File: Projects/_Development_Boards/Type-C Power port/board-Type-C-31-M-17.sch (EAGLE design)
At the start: 2 parts, among them J1 TYPE-C-31-M-17

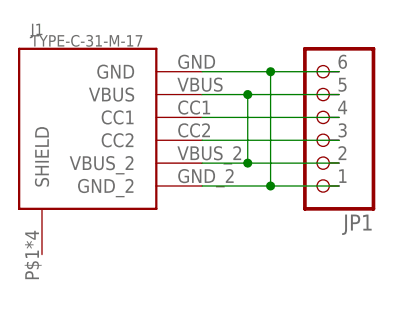
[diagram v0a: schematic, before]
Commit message: Type-C power port PCB panelized
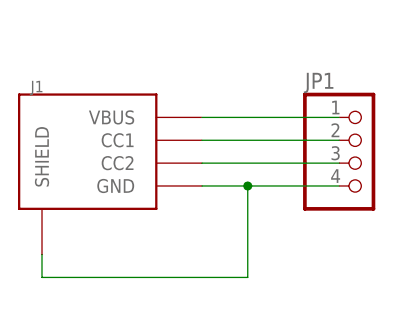
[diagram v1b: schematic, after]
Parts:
- J1: value TYPE-C-31-M-17 -> USB-TYPE-C-31-M-17; device angrypig7_Library:TYPE-C-31-M-17 -> angrypig7-Connectors:USB-TYPE-C-31-M-17
- JP1: device pinhead_v2:PINHD-1X6/OCT -> pinhead_v2:PINHD-1X4/OCT
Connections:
- net N$1: now also J1.GND, J1.SHIELD, JP1.4; no longer J1.VBUS, J1.VBUS_2, JP1.2, JP1.5
- net N$2: now also J1.VBUS; no longer J1.GND, J1.GND_2, JP1.6
- net N$3: now also JP1.2; no longer JP1.4
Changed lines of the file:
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@@
 <?xml version="1.0" encoding="utf-8"?>
 <!DOCTYPE eagle SYSTEM "eagle.dtd">
-<eagle version="9.5.2">
+<eagle version="9.6.0">
 <drawing>
 <settings>
-<setting alwaysvectorfont="yes"/>
+<setting alwaysvectorfont="no"/>
 <setting verticaltext="up"/>
 </settings>
@@
 <layer number="128" name="_bValues" color="7" fill="1" visible="no" active="no"/>
 <layer number="129" name="Mask" color="7" fill="1" visible="no" active="no"/>
+<layer number="130" name="SMDSTROOK" color="7" fill="1" visible="no" active="no"/>
 <layer number="131" name="tAdjust" color="7" fill="1" visible="no" active="no"/>
 <layer number="132" name="bAdjust" color="7" fill="1" visible="no" active="no"/>
+<layer number="133" name="bottom_silk" color="7" fill="1" visible="no" active="no"/>
+<layer number="134" name="silk_top" color="7" fill="1" visible="no" active="no"/>
+<layer number="135" name="silk_bottom" color="7" fill="1" visible="no" active="no"/>
+<layer number="136" name="silktop" color="7" fill="1" visible="no" active="yes"/>
+<layer number="137" name="silkbottom" color="7" fill="1" visible="no" active="yes"/>
 <layer number="144" name="Drill_legend" color="7" fill="1" visible="no" active="no"/>
+<layer number="145" name="DrillLegend_01-16" color="7" fill="1" visible="no" active="yes"/>
+<layer number="146" name="DrillLegend_01-20" color="7" fill="1" visible="no" active="yes"/>
 <layer number="150" name="Notes" color="7" fill="1" visible="no" active="no"/>
 <layer number="151" name="HeatSink" color="7" fill="1" visible="no" active="no"/>
@@
 <layer number="154" name="FabDoc2" color="7" fill="1" visible="no" active="no"/>
 <layer number="155" name="FabDoc3" color="7" fill="1" visible="no" active="no"/>
+<layer number="166" name="AntennaArea" color="7" fill="1" visible="no" active="yes"/>
+<layer number="168" name="4mmHeightArea" color="7" fill="1" visible="no" active="yes"/>
 <layer number="199" name="Contour" color="7" fill="1" visible="no" active="no"/>
 <layer number="200" name="200bmp" color="1" fill="10" visible="no" active="no"/>
@@
 </variantdefs>
 <classes>
-<class number="0" name="default" width="0" drill="0">
+<class number="0" name="default" width="0.254" drill="0">
+</class>
+<class number="1" name="power" width="0.4572" drill="0">
 </class>
 </classes>
 <parts>
-<part name="J1" library="angrypig7_Library" deviceset="TYPE-C-31-M-17" device=""/>
-<part name="JP1" library="pinhead_v2" deviceset="PINHD-1X6" device="/OCT"/>
+<part name="J1" library="angrypig7-Connectors" deviceset="USB-TYPE-C-31-M-17" device=""/>
+<part name="JP1" library="pinhead_v2" deviceset="PINHD-1X4" device="/OCT"/>
 </parts>
 <sheets>
@@
 </plain>
 <instances>
-<instance part="J1" gate="G$1" x="7.62" y="25.4" smashed="yes">
-<attribute name="NAME" x="6.35" y="34.544" size="1.27" layer="95"/>
-<attribute name="VALUE" x="6.35" y="33.274" size="1.27" layer="95"/>
+<instance part="J1" gate="G$1" x="7.62" y="20.32" smashed="yes">
+<attribute name="NAME" x="6.35" y="28.194" size="1.27" layer="95"/>
 </instance>
-<instance part="JP1" gate="A" x="38.1" y="25.4" smashed="yes" rot="R180">
-<attribute name="NAME" x="44.45" y="14.605" size="1.778" layer="95" rot="R180"/>
-<attribute name="VALUE" x="44.45" y="35.56" size="1.778" layer="96" rot="R180"/>
+<instance part="JP1" gate="A" x="43.18" y="20.32" smashed="yes">
+<attribute name="NAME" x="36.83" y="28.575" size="1.778" layer="95"/>
+<attribute name="VALUE" x="36.83" y="12.7" size="1.778" layer="96"/>
 </instance>
 </instances>
@@
 </busses>
 <nets>
-<net name="N$1" class="0">
+<net name="N$1" class="1">
+<segment>
+<pinref part="J1" gate="G$1" pin="SHIELD"/>
+<wire x1="7.62" y1="10.16" x2="7.62" y2="7.62" width="0.1524" layer="91"/>
+<wire x1="7.62" y1="7.62" x2="30.48" y2="7.62" width="0.1524" layer="91"/>
+<wire x1="30.48" y1="7.62" x2="30.48" y2="17.78" width="0.1524" layer="91"/>
+<pinref part="J1" gate="G$1" pin="GND"/>
+<wire x1="30.48" y1="17.78" x2="25.4" y2="17.78" width="0.1524" layer="91"/>
+<pinref part="JP1" gate="A" pin="4"/>
+<wire x1="30.48" y1="17.78" x2="40.64" y2="17.78" width="0.1524" layer="91"/>
+<junction x="30.48" y="17.78"/>
+</segment>
+</net>
+<net name="N$2" class="1">
 <segment>
 <pinref part="J1" gate="G$1" pin="VBUS"/>
-<wire x1="25.4" y1="27.94" x2="30.48" y2="27.94" width="0.1524" layer="91"/>
-<wire x1="30.48" y1="27.94" x2="30.48" y2="20.32" width="0.1524" layer="91"/>
-<pinref part="J1" gate="G$1" pin="VBUS_2"/>
-<wire x1="30.48" y1="20.32" x2="25.4" y2="20.32" width="0.1524" layer="91"/>
-<pinref part="JP1" gate="A" pin="5"/>
-<wire x1="30.48" y1="27.94" x2="40.64" y2="27.94" width="0.1524" layer="91"/>
-<junction x="30.48" y="27.94"/>
+<pinref part="JP1" gate="A" pin="1"/>
+<wire x1="25.4" y1="25.4" x2="40.64" y2="25.4" width="0.1524" layer="91"/>
+</segment>
+</net>
+<net name="N$3" class="0">
+<segment>
+<pinref part="J1" gate="G$1" pin="CC1"/>
 <pinref part="JP1" gate="A" pin="2"/>
-<wire x1="40.64" y1="20.32" x2="30.48" y2="20.32" width="0.1524" layer="91"/>
-<junction x="30.48" y="20.32"/>
-</segment>
-</net>
-<net name="N$2" class="0">
-<segment>
-<pinref part="J1" gate="G$1" pin="GND_2"/>
-<wire x1="25.4" y1="17.78" x2="33.02" y2="17.78" width="0.1524" layer="91"/>
-<wire x1="33.02" y1="17.78" x2="33.02" y2="30.48" width="0.1524" layer="91"/>
-<pinref part="J1" gate="G$1" pin="GND"/>
-<wire x1="33.02" y1="30.48" x2="25.4" y2="30.48" width="0.1524" layer="91"/>
-<pinref part="JP1" gate="A" pin="6"/>
-<wire x1="40.64" y1="30.48" x2="33.02" y2="30.48" width="0.1524" layer="91"/>
-<junction x="33.02" y="30.48"/>
-<pinref part="JP1" gate="A" pin="1"/>
-<wire x1="33.02" y1="17.78" x2="40.64" y2="17.78" width="0.1524" layer="91"/>
-<junction x="33.02" y="17.78"/>
-</segment>
-</net>
-<net name="N$3" class="0">
-<segment>
-<pinref part="JP1" gate="A" pin="4"/>
-<pinref part="J1" gate="G$1" pin="CC1"/>
-<wire x1="40.64" y1="25.4" x2="25.4" y2="25.4" width="0.1524" layer="91"/>
+<wire x1="25.4" y1="22.86" x2="40.64" y2="22.86" width="0.1524" layer="91"/>
 </segment>
 </net>
@@
 <pinref part="J1" gate="G$1" pin="CC2"/>
 <pinref part="JP1" gate="A" pin="3"/>
-<wire x1="25.4" y1="22.86" x2="40.64" y2="22.86" width="0.1524" layer="91"/>
-</segment>
-</net>
+<wire x1="25.4" y1="20.32" x2="40.64" y2="20.32" width="0.1524" layer="91"/>
+</segment>
+</net>
